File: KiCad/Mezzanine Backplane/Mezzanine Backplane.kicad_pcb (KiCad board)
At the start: 4 copper layers, 29.1 x 85 mm, 9 parts, among them J1 BB0500220F-1002C-001, J2 BB0500220F-1002C-001, J3 Conn_02x25_Odd_Even, J4 Conn_02x25_Odd_Even

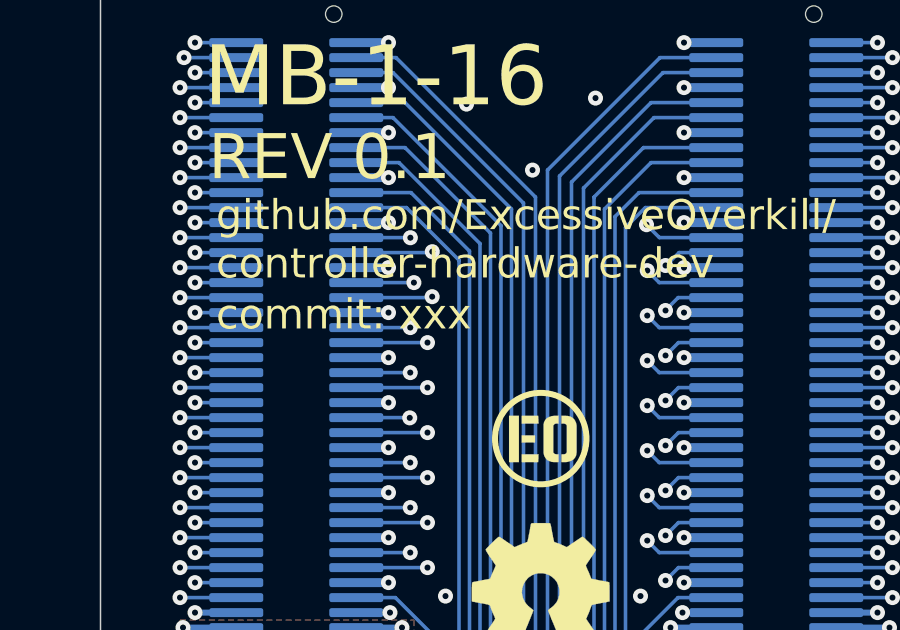
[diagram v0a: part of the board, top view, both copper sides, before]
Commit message: fix jumper
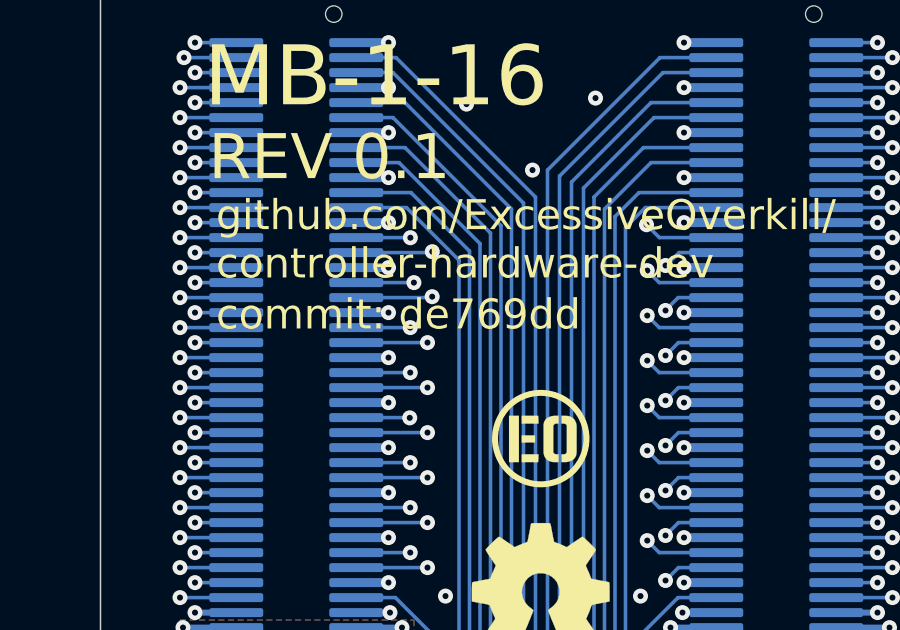
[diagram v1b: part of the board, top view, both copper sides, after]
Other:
- board text added: "commit: de769dd"
- board text removed: "commit: xxx"
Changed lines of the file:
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@@
 			(psa4output no)
 			(plotreference yes)
-			(plotvalue yes)
+			(plotvalue no)
 			(plotfptext yes)
 			(plotinvisibletext no)
@@
 			(outputformat 1)
 			(mirror no)
-			(drillshape 1)
+			(drillshape 0)
 			(scaleselection 1)
-			(outputdirectory "")
+			(outputdirectory "manufacturing outputs/")
 		)
 	)
@@
 		)
 	)
-	(gr_text "commit: xxx"
-		(at 77.45 97.4 -0)
+	(gr_text "commit: de769dd"
+		(at 77.45 97.4 0)
 		(layer "F.SilkS")
 		(effects
